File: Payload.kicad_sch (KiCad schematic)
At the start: 1 part, among them U1 STM32-(STM32H745ZIT6)

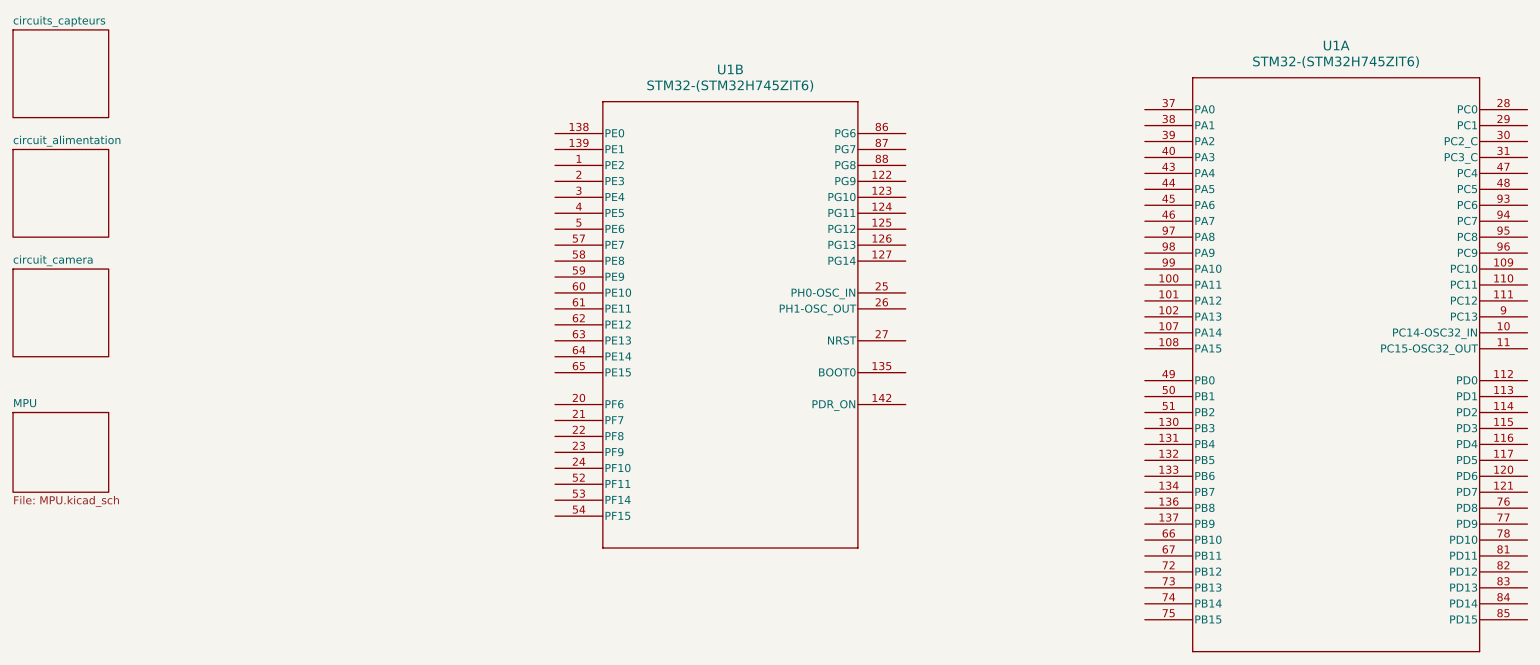
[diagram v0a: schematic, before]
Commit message: Recommit du Vbuck
On réessaye de commit parce que ça a pas marché...

Le régulateur de tension buck converter a été ajouté au payload dans la page Vbuck qui remplace la page circuit caméras.
J'ai enlevé la switch du buck et connecté l'entré on/off à GND.
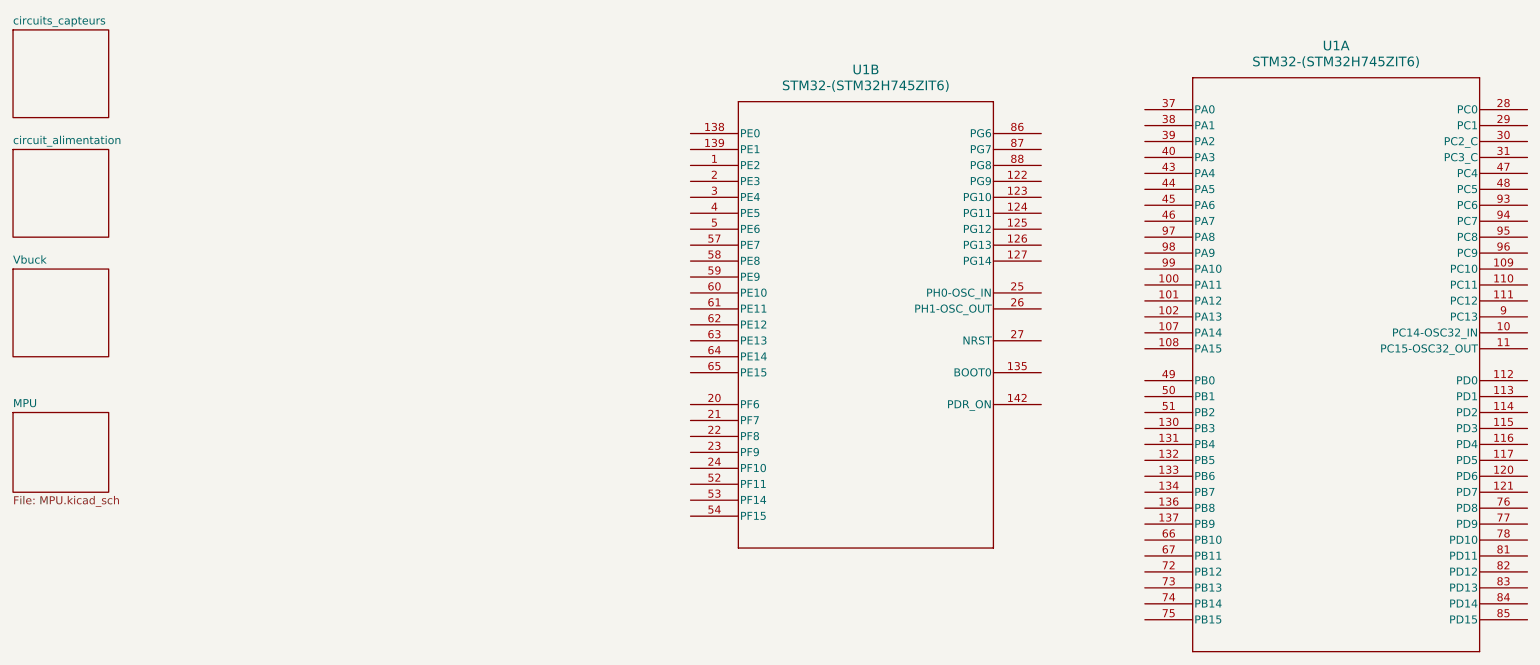
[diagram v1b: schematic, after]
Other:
- sheet circuit_camera renamed Vbuck
- moved on the sheet: U1B

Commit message: Revert "Recommit du Vbuck"
This reverts commit db6b1385e92bec759ec8c6f30127fdc08b8b4918.
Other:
- sheet Vbuck renamed circuit_camera
- moved on the sheet: U1B
